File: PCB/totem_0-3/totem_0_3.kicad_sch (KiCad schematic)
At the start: 88 parts, among them J1 MJ-4PP-9, J2 MJ-4PP-9, U1 xiao-ble, U2 xiao-ble

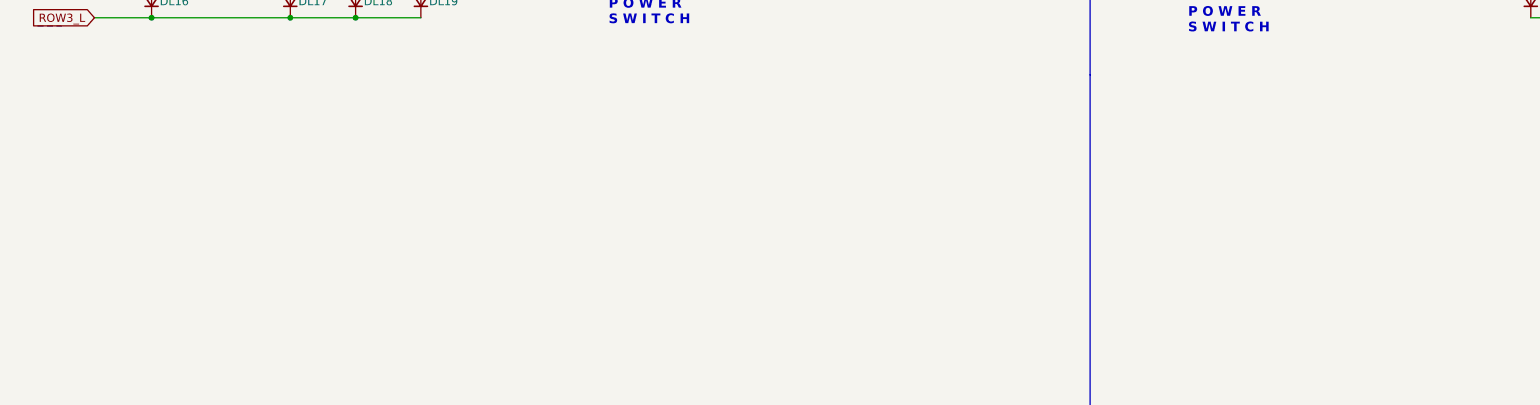
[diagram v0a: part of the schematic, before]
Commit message: pcb: add trackpoint mounting hole
Signed-off-by: Anant Thazhemadam <anant.thazhemadam@gmail.com>
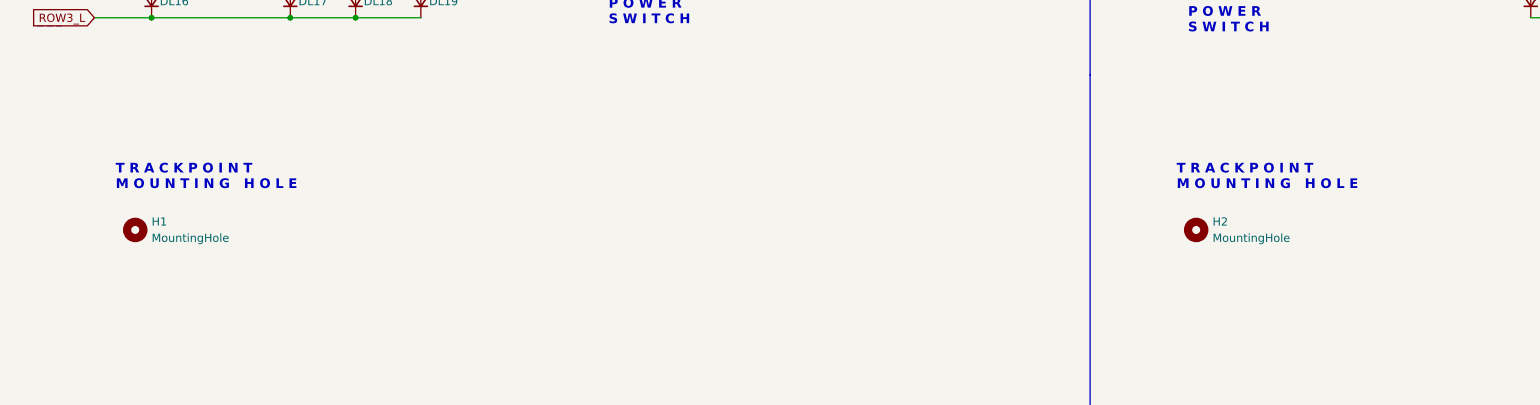
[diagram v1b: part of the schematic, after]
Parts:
- added H1, H2: MountingHole, TOTEMlib:TPSensorModule, symbol Mechanical:MountingHole
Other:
- note added: "T R A C K P O I N T M O U N T I N G H O L E"
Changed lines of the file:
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@@
 		)
 	)
+	(text "T R A C K P O I N T\nM O U N T I N G   H O L E"
+		(exclude_from_sim no)
+		(at 198.882 186.944 0)
+		(effects
+			(font
+				(size 1.5 1.5)
+				(thickness 0.3)
+				(bold yes)
+			)
+			(justify left bottom)
+		)
+	)
 	(text "M I C R O \nC O N T R O L L E R"
 		(exclude_from_sim no)
@@
 		)
 	)
+	(text "T R A C K P O I N T\nM O U N T I N G   H O L E"
+		(exclude_from_sim no)
+		(at 33.782 186.944 0)
+		(effects
+			(font
+				(size 1.5 1.5)
+				(thickness 0.3)
+				(bold yes)
+			)
+			(justify left bottom)
+		)
+	)
 	(text "S W I T C H\nM A T R I X"
 		(exclude_from_sim no)
@@
 	)
 	(symbol
+		(lib_id "Mechanical:MountingHole")
+		(at 36.83 193.04 0)
+		(unit 1)
+		(exclude_from_sim yes)
+		(in_bom no)
+		(on_board yes)
+		(dnp no)
+		(fields_autoplaced yes)
+		(property "Reference" "H1"
+			(at 39.37 191.7699 0)
+			(effects
+				(font
+					(size 1.27 1.27)
+				)
+				(justify left)
+			)
+		)
+		(property "Value" "MountingHole"
+			(at 39.37 194.3099 0)
+			(effects
+				(font
+					(size 1.27 1.27)
+				)
+				(justify left)
+			)
+		)
+		(property "Footprint" "TOTEMlib:TPSensorModule"
+			(at 36.83 193.04 0)
+			(effects
+				(font
+					(size 1.27 1.27)
+				)
+				(hide yes)
+			)
+		)
+		(property "Datasheet" "~"
+			(at 36.83 193.04 0)
+			(effects
+				(font
+					(size 1.27 1.27)
+				)
+				(hide yes)
+			)
+		)
+		(property "Description" "Mounting Hole without connection"
+			(at 36.83 193.04 0)
+			(effects
+				(font
+					(size 1.27 1.27)
+				)
+				(hide yes)
+			)
+		)
+		(instances
+			(project "totem_0_3"
+				(path "/4d1e609f-5432-4afb-8ee7-7d2d9aaaee48"
+					(reference "H1")
+					(unit 1)
+				)
+			)
+		)
+	)
+	(symbol
 		(lib_id "Switch:SW_Push_45deg")
 		(at 271.78 123.19 0)
@@
 					(unit 1)
 				)
+			)
+		)
+	)
+	(symbol
+		(lib_id "Mechanical:MountingHole")
+		(at 201.93 193.04 0)
+		(unit 1)
+		(exclude_from_sim yes)
+		(in_bom no)
+		(on_board yes)
+		(dnp no)
+		(fields_autoplaced yes)
+		(property "Reference" "H2"
+			(at 204.47 191.7699 0)
+			(effects
+				(font
+					(size 1.27 1.27)
+				)
+				(justify left)
+			)
+		)
+		(property "Value" "MountingHole"
+			(at 204.47 194.3099 0)
+			(effects
+				(font
+					(size 1.27 1.27)
+				)
+				(justify left)
+			)
+		)
+		(property "Footprint" "TOTEMlib:TPSensorModule"
+			(at 201.93 193.04 0)
+			(effects
+				(font
+					(size 1.27 1.27)
+				)
+				(hide yes)
+			)
+		)
+		(property "Datasheet" "~"
+			(at 201.93 193.04 0)
+			(effects
+				(font
+					(size 1.27 1.27)
+				)
+				(hide yes)
+			)
+		)
+		(property "Description" "Mounting Hole without connection"
+			(at 201.93 193.04 0)
+			(effects
+				(font
+					(size 1.27 1.27)
+				)
+				(hide yes)
+			)
+		)
+		(instances
+			(project "totem_0_3"
+				(path "/4d1e609f-5432-4afb-8ee7-7d2d9aaaee48"
+					(reference "H2")
+					(unit 1)
+				)

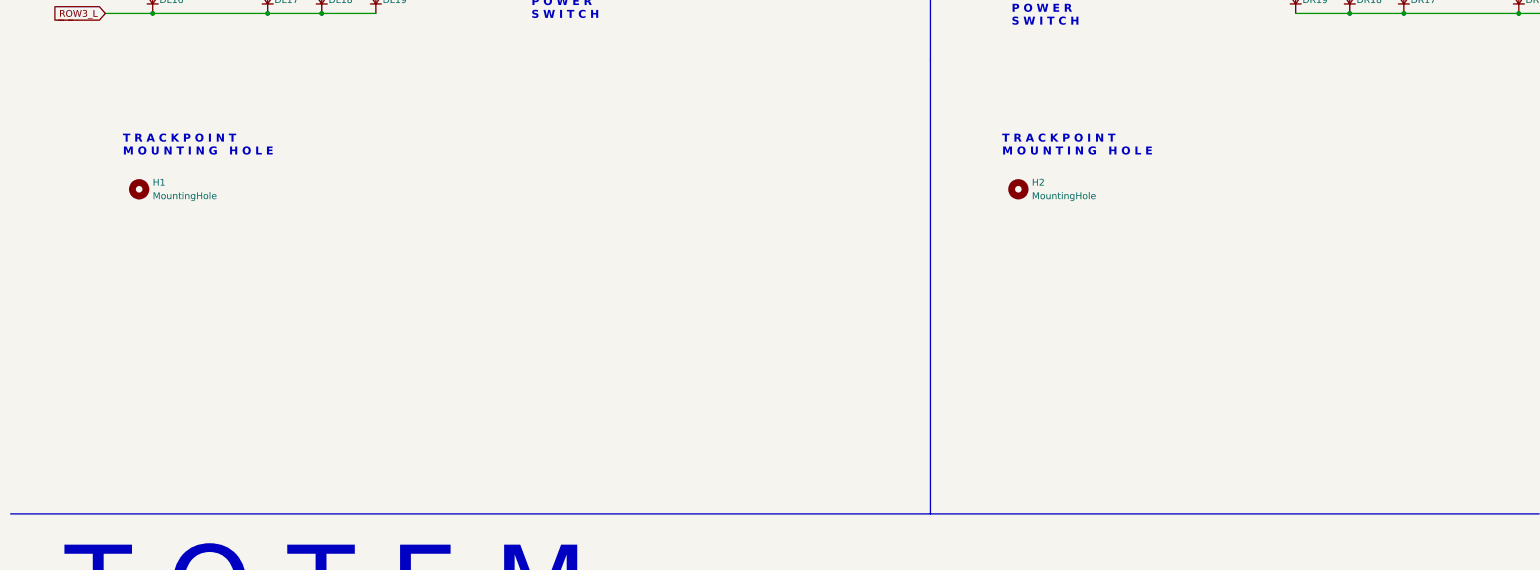
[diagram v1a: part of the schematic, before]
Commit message: sch: add (unconnected) symbols of shift register, trackpoint & breakout
Signed-off-by: Anant Thazhemadam <anant.thazhemadam@gmail.com>
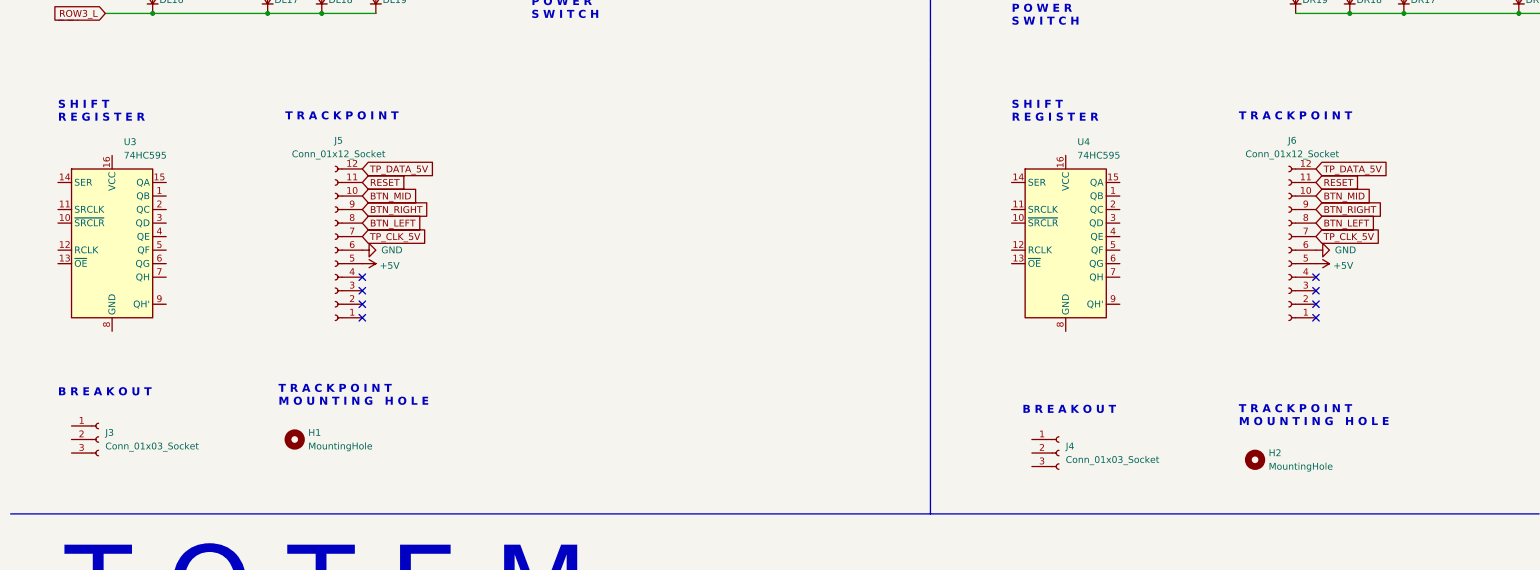
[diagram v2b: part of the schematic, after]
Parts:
- added J3, J4: Conn_01x03_Socket, Connector_PinHeader_2.54mm:PinHeader_1x03_P2.54mm_Vertical, symbol Connector:Conn_01x03_Socket
- added J5, J6: Conn_01x12_Socket, Connector_FFC-FPC:TE_1-84953-2_1x12-1MP_P1.0mm_Horizontal, symbol Connector:Conn_01x12_Socket
- added U3, U4: 74HC595, Package_SO:SOIC-16_3.9x9.9mm_P1.27mm, symbol 74xx:74HC595
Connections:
- new net +5V: J5.5 (Pin_5), J6.5 (Pin_5)
- new net BTN_LEFT: J5.8 (Pin_8), J6.8 (Pin_8)
- new net BTN_MID: J5.10 (Pin_10), J6.10 (Pin_10)
- new net BTN_RIGHT: J5.9 (Pin_9), J6.9 (Pin_9)
- new net GND: J5.6 (Pin_6), J6.6 (Pin_6)
- new net RESET: J5.11 (Pin_11), J6.11 (Pin_11)
- new net TP_CLK_5V: J5.7 (Pin_7), J6.7 (Pin_7)
- new net TP_DATA_5V: J5.12 (Pin_12), J6.12 (Pin_12)
- no-connect marks 12 -> 20
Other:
- note added: "B R E A K O U T"
- note added: "S H I F T R E G I S T E R"
- note added: "T R A C K P O I N T"

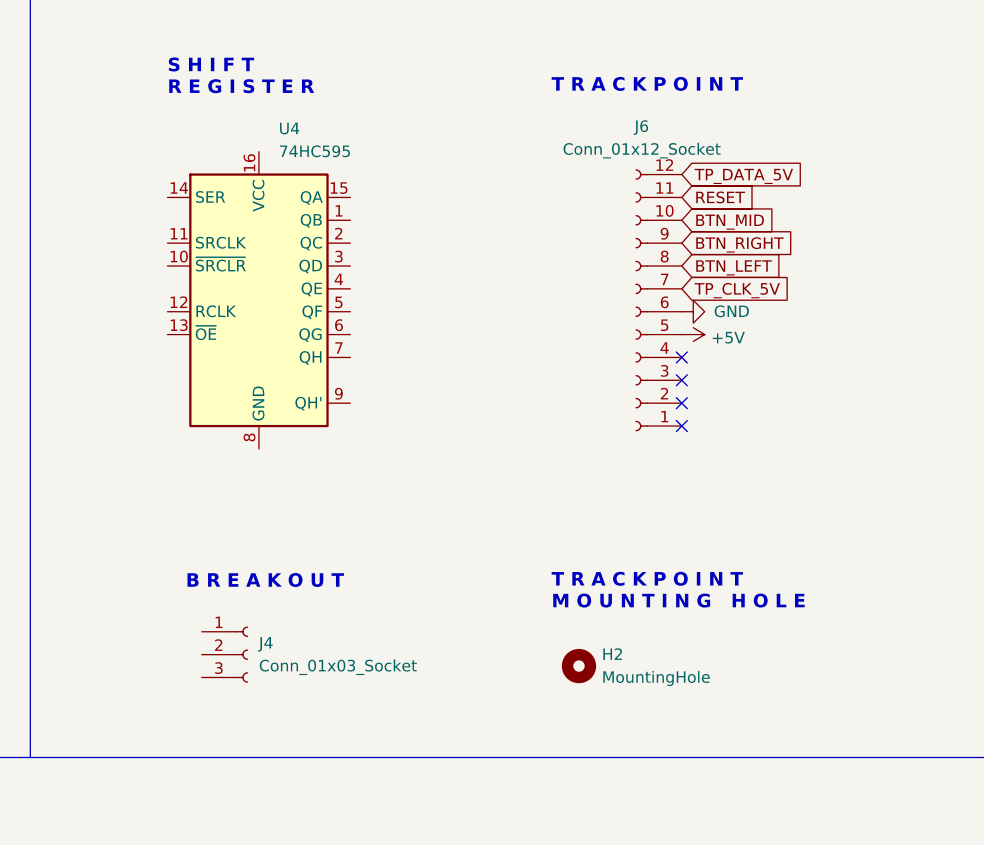
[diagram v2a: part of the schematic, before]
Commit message: sch: annotate all lhs components with no-wire
Signed-off-by: Anant Thazhemadam <anant.thazhemadam@gmail.com>
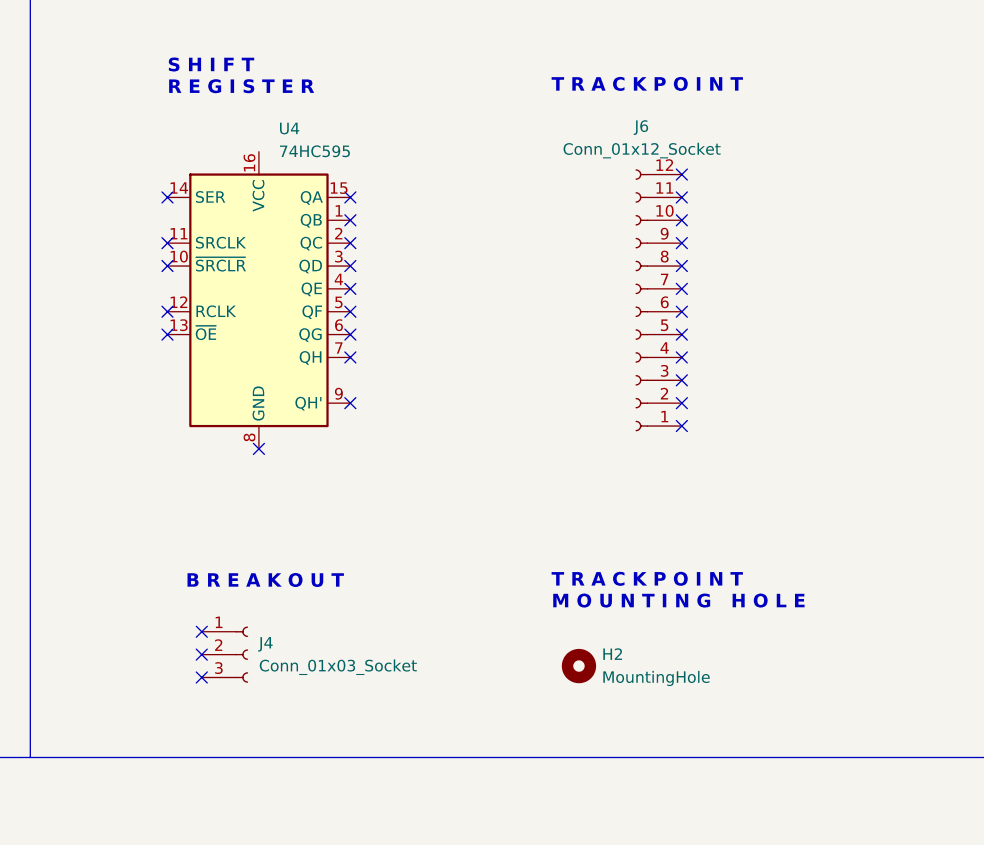
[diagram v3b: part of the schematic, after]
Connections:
- net +5V: no longer J6.5 (Pin_5)
- net BTN_LEFT: no longer J6.8 (Pin_8)
- net BTN_MID: no longer J6.10 (Pin_10)
- net BTN_RIGHT: no longer J6.9 (Pin_9)
- net GND: no longer J6.6 (Pin_6)
- net RESET: no longer J6.11 (Pin_11)
- net TP_CLK_5V: no longer J6.7 (Pin_7)
- net TP_DATA_5V: no longer J6.12 (Pin_12)
- no-connect marks 20 -> 46
